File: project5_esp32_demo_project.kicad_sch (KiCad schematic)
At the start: 25 parts, among them J1 SS-52400-002, J2 B2B-PH-SM4-TB, U1 MCP73871-2CAI_ML

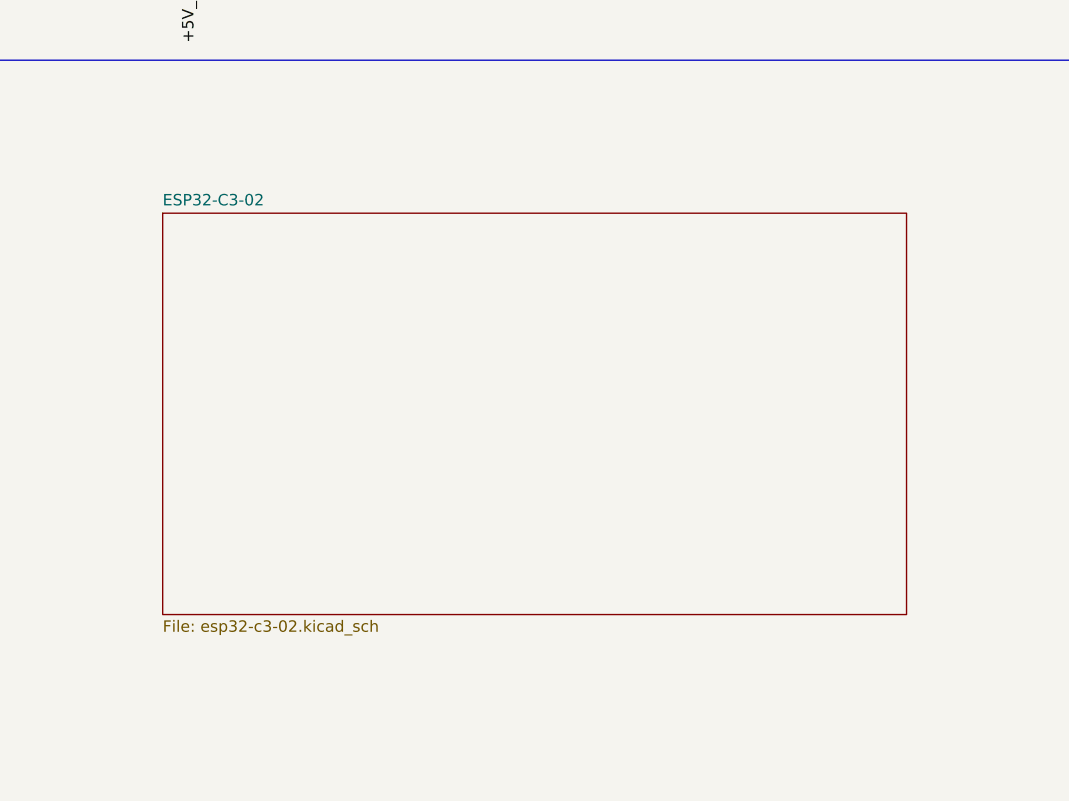
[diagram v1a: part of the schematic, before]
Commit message: 1.2.1 Design the USB to UART bridge subcircuit
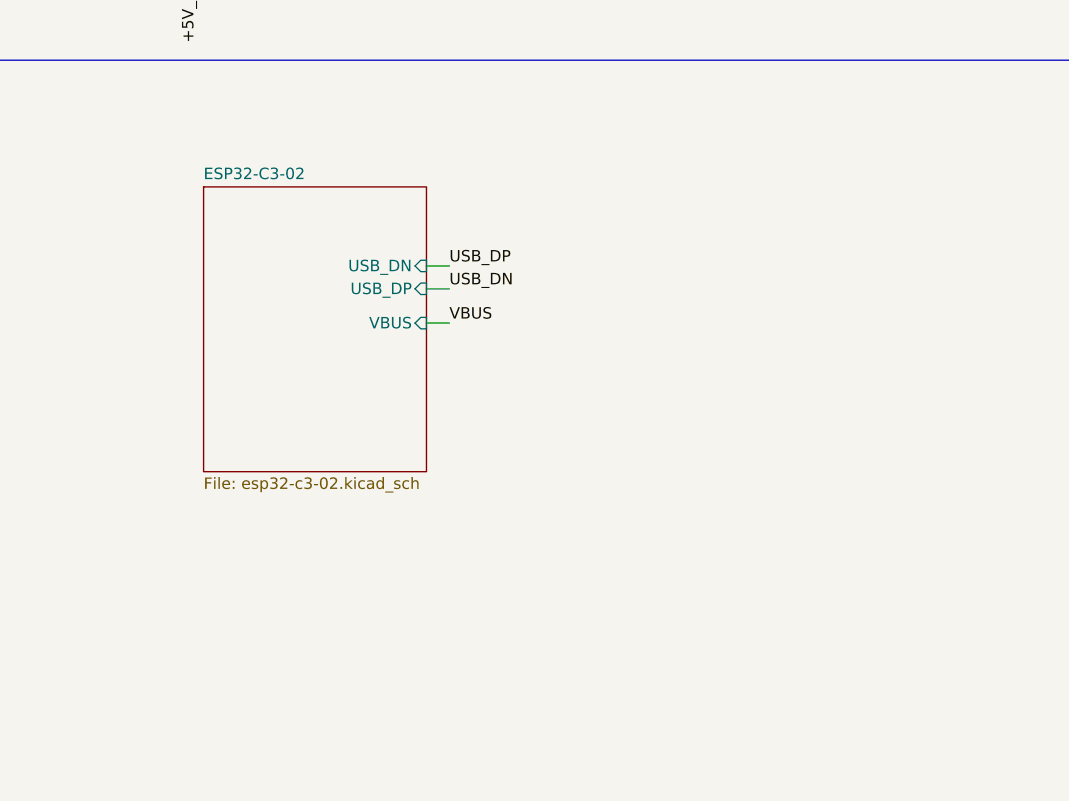
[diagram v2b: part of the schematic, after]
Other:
- sheet ESP32-C3-02 ports: added USB_DN, USB_DP, VBUS; removed none
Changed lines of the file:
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@@
 	(wire
 		(pts
+			(xy 191.77 124.46) (xy 194.31 124.46)
+		)
+		(stroke
+			(width 0)
+			(type default)
+		)
+	)
+	(wire
+		(pts
 			(xy 115.57 118.11) (xy 115.57 113.03)
 		)
@@
 	(wire
 		(pts
+			(xy 191.77 118.11) (xy 194.31 118.11)
+		)
+		(stroke
+			(width 0)
+			(type default)
+		)
+	)
+	(wire
+		(pts
 			(xy 259.08 44.45) (xy 261.62 44.45)
 		)
@@
 	(wire
 		(pts
+			(xy 191.77 120.65) (xy 194.31 120.65)
+		)
+		(stroke
+			(width 0)
+			(type default)
+		)
+	)
+	(wire
+		(pts
 			(xy 166.37 80.645) (xy 166.37 85.09)
 		)
@@
 		)
 	)
+	(label "USB_DP"
+		(at 194.31 118.11 0)
+		(effects
+			(font
+				(size 1.27 1.27)
+			)
+			(justify left bottom)
+		)
+	)
+	(label "USB_DN"
+		(at 194.31 120.65 0)
+		(effects
+			(font
+				(size 1.27 1.27)
+			)
+			(justify left bottom)
+		)
+	)
+	(label "VBUS"
+		(at 194.31 124.46 0)
+		(effects
+			(font
+				(size 1.27 1.27)
+			)
+			(justify left bottom)
+		)
+	)
 	(label "CHARGING"
 		(at 179.07 49.53 90)
@@
 	)
 	(sheet
-		(at 162.46 112.25)
-		(size 82.65 44.595)
+		(at 167.005 109.33)
+		(size 24.765 31.64)
 		(exclude_from_sim no)
 		(in_bom yes)
@@
 		)
 		(property "Sheetname" "ESP32-C3-02"
-			(at 162.46 111.5384 0)
+			(at 167.005 108.6184 0)
 			(effects
 				(font
@@
 		)
 		(property "Sheetfile" "esp32-c3-02.kicad_sch"
-			(at 162.46 157.4296 0)
+			(at 167.005 141.5546 0)
 			(effects
 				(font
@@
 			)
 		)
+		(pin "USB_DN" input
+			(at 191.77 118.11 0)
+			(effects
+				(font
+					(size 1.27 1.27)
+				)
+				(justify right)
+			)
+		)
+		(pin "USB_DP" input
+			(at 191.77 120.65 0)
+			(effects
+				(font
+					(size 1.27 1.27)
+				)
+				(justify right)
+			)
+		)
+		(pin "VBUS" input
+			(at 191.77 124.46 0)
+			(effects
+				(font
+					(size 1.27 1.27)
+				)
+				(justify right)
+			)
+		)

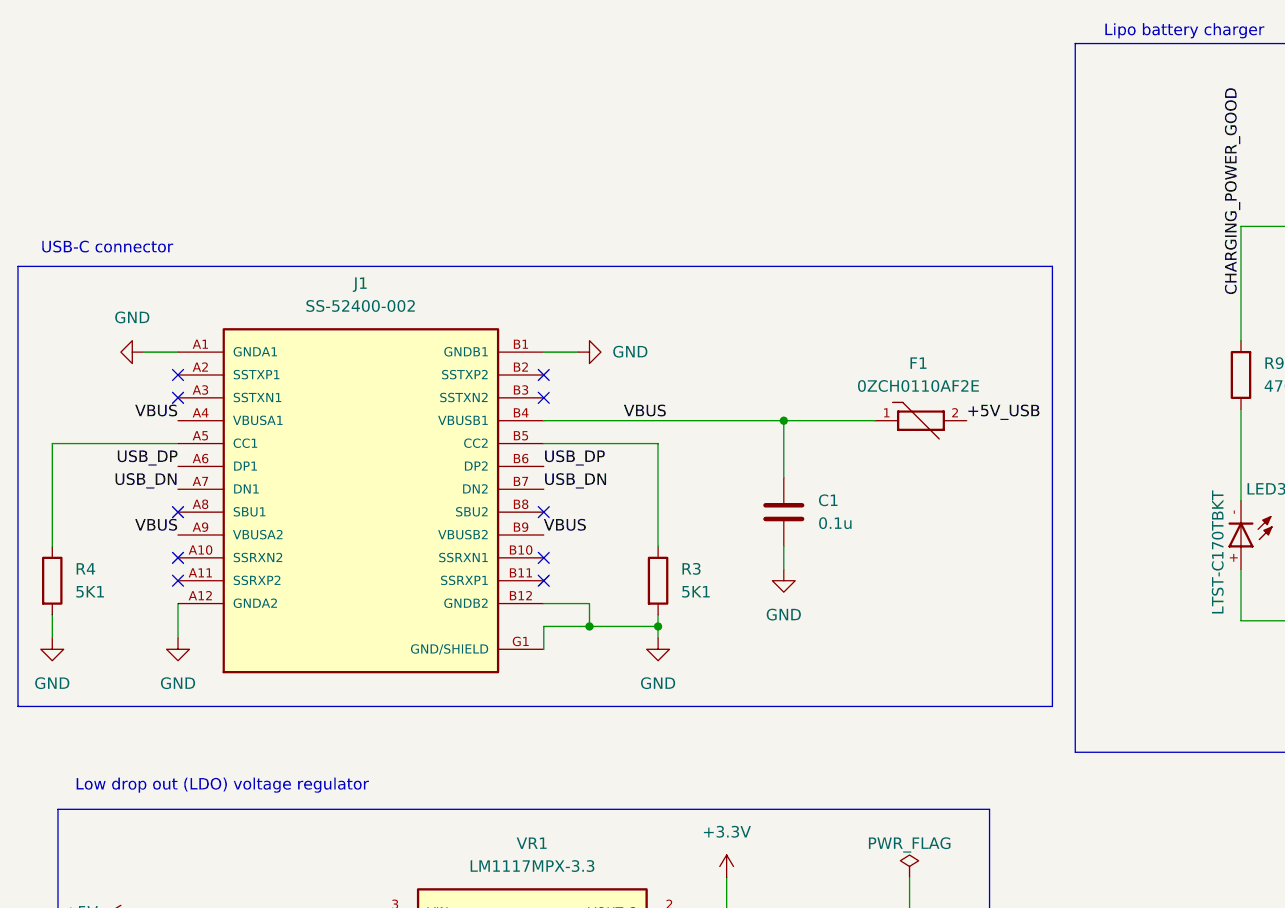
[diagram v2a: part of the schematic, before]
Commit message: 1.3.3 Symbol and footprint associations
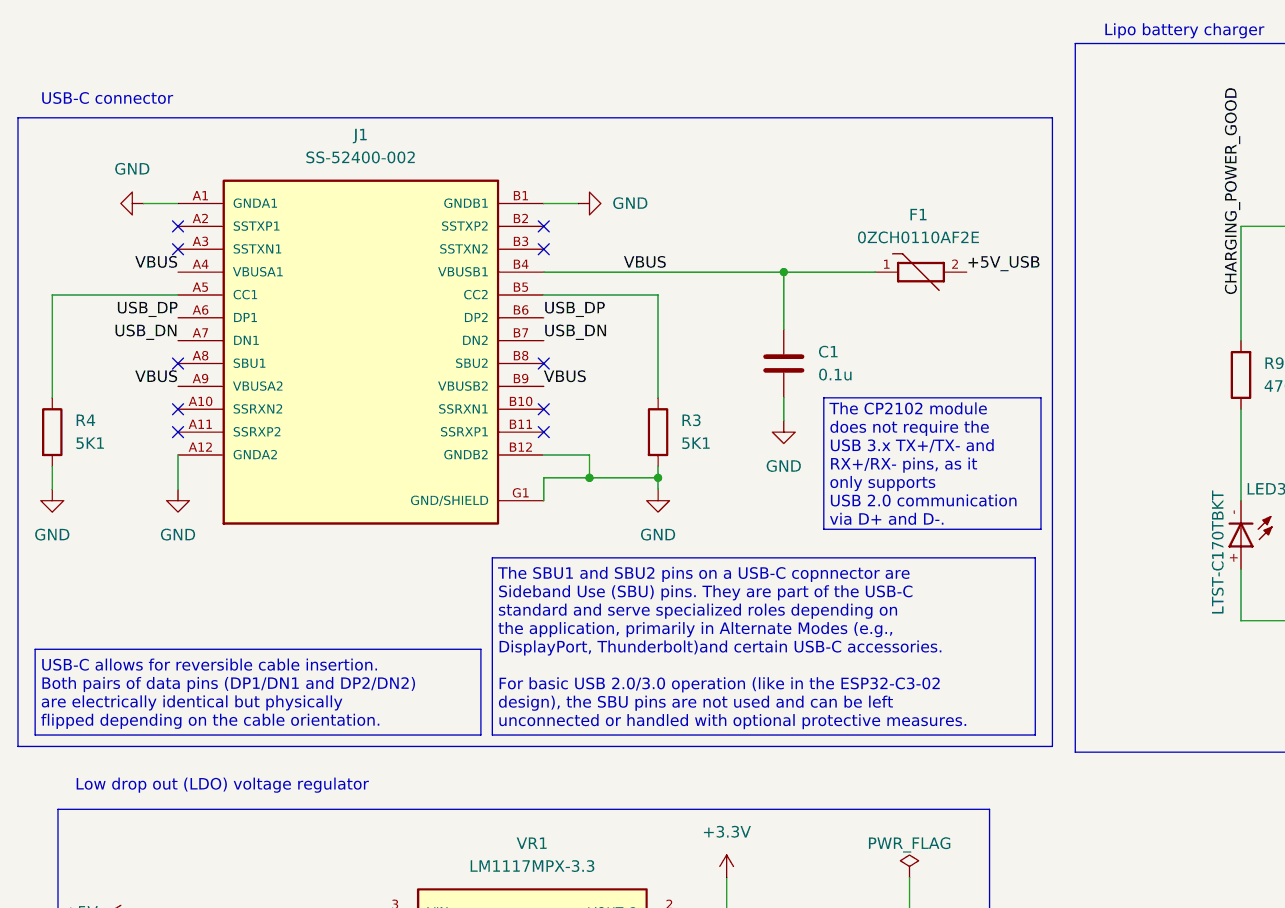
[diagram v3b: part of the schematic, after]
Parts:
- C1, C2, C5, C6: footprint (none) -> Capacitor_SMD:C_0805_2012Metric
- C3, C4: footprint (none) -> ESP32_demo_project:T491A106K010AT7280
- LED2, LED4: footprint LED_LTST-C170GKT_LTO -> (none)
- R1, R10, R2, R3, R4, R5, R6, R7, R8, R9: footprint (none) -> Resistor_SMD:R_0805_2012Metric
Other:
- note added: "The CP2102 module does not require the USB 3.x TX+/TX- and RX+/RX- pins, as it only supports USB 2.0 communication via D+ and D-."
- note added: "The SBU1 and SBU2 pins on a USB-C copnnector are Sideband Use (SBU) pins. They are part of the USB-C standard and serve specialized roles depending on the application, primarily in Alternate Modes (e.g., DisplayPort, Thunderbolt)and certain USB-C accessories. For basic USB 2.0/3.0 operation (like in the ESP32-C3-02 design), the SBU pins are not used and can be left unconnected or handled with opt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"
- note added: "USB-C allows for reversible cable insertion. Both pairs of data pins (DP1/DN1 and DP2/DN2) are electrically identical but physically flipped depending on the cable orientation."
- moved on the sheet: C1, F1, J1, R3, R4

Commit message: 1.3.4 Electrical Rules Check
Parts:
- F1: footprint 0ZCH0110AF2E:FUSC3225X100N -> ESP32_demo_project:0ZCH0110AF2E
- J1: footprint SS-52400-002:BELFUSE_SS-52400-002 -> ESP32_demo_project:SS-52400-002
- VR1: footprint LM1117MPX-3.3:VREG_LM1117MPX-3.3 -> ESP32_demo_project:LM1117MPX-3.3
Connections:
- net GND: now also U1.3 (SEL)
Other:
- moved on the sheet: F1

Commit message: 1.3.9 Bring remaining components to the layout editor
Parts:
- J2: footprint B2B-PH-SM4-TB:JST_B2B-PH-SM4-TB -> ESP32_demo_project:B2B-PH-SM4-TB
- LED1: footprint LTST-C170KRKT:DIOC200X125X110 -> ESP32_demo_project:LTST-C170KRKT
- LED2, LED4: footprint (none) -> ESP32_demo_project:LTST-C170GKT
- LED3: footprint LTST-C170TBKT:DIOC200X125X110 -> ESP32_demo_project:LTST-C170TBKT
- U1: footprint MCP73871-2CAI_ML:QFN50P400X400X100-21N -> ESP32_demo_project:MCP73871-2CAI_ML
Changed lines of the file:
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@@
 			)
 		)
-		(property "Footprint" ""
+		(property "Footprint" "ESP32_demo_project:LTST-C170GKT"
 			(at 166.37 74.93 0)
 			(effects
@@
 			)
 		)
-		(property "Footprint" ""
+		(property "Footprint" "ESP32_demo_project:LTST-C170GKT"
 			(at 92.71 173.99 0)
 			(effects
@@
 			)
 		)
-		(property "Footprint" "LTST-C170TBKT:DIOC200X125X110"
+		(property "Footprint" "ESP32_demo_project:LTST-C170TBKT"
 			(at 152.4 69.85 0)
 			(effects
@@
 			)
 		)
-		(property "Footprint" "MCP73871-2CAI_ML:QFN50P400X400X100-21N"
+		(property "Footprint" "ESP32_demo_project:MCP73871-2CAI_ML"
 			(at 226.06 41.91 0)
 			(effects
@@
 			)
 		)
-		(property "Footprint" "B2B-PH-SM4-TB:JST_B2B-PH-SM4-TB"
+		(property "Footprint" "ESP32_demo_project:B2B-PH-SM4-TB"
 			(at 45.72 165.1 0)
 			(effects
@@
 				)
 				(justify bottom)
+				(hide yes)
+			)
+		)
+		(property "Purpose" ""
+			(at 45.72 165.1 0)
+			(effects
+				(font
+					(size 1.27 1.27)
+				)
 				(hide yes)
 			)
@@
 			)
 		)
-		(property "Footprint" "LTST-C170KRKT:DIOC200X125X110"
+		(property "Footprint" "ESP32_demo_project:LTST-C170KRKT"
 			(at 179.07 68.58 0)
 			(effects
